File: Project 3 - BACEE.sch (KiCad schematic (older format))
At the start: 13 parts, among them U1 DS1337_PDv1, U2 24LC1025, U3 24LC1025, U4 ATMEGA328P-AU, Y1 Crystal, Y2 Crystal

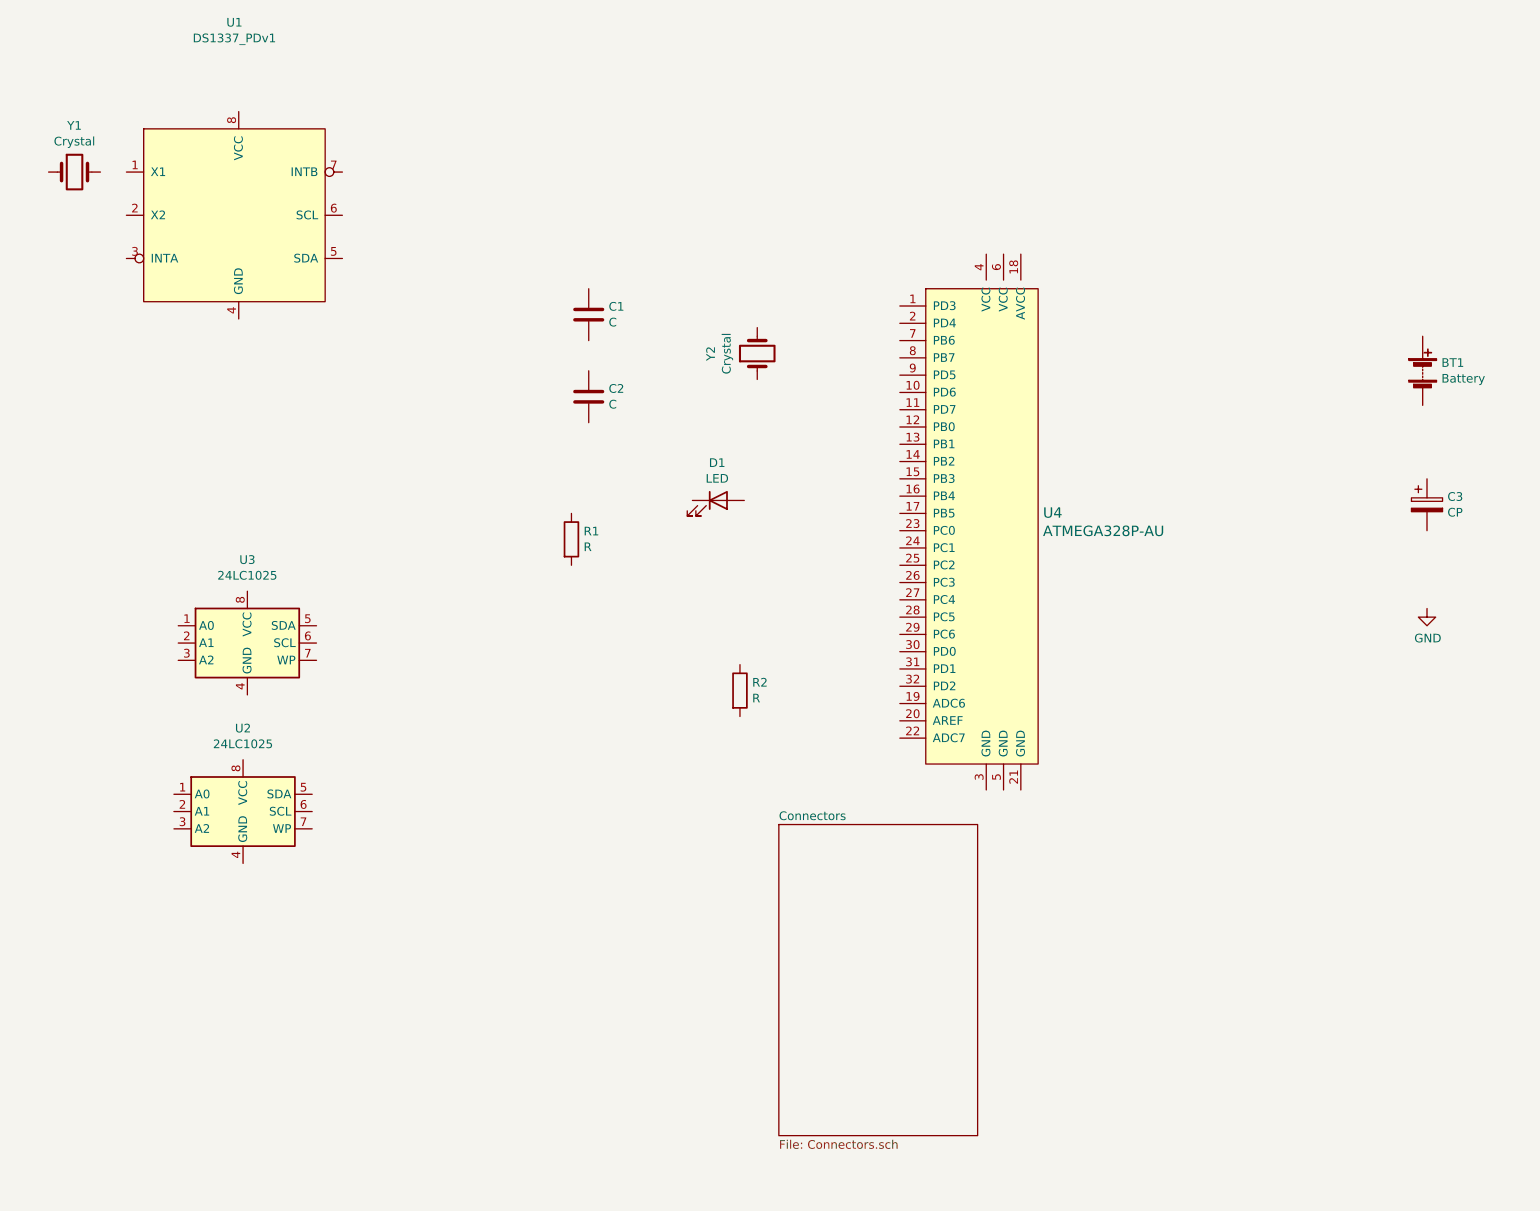
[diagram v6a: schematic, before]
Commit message: Completed association and added component values.
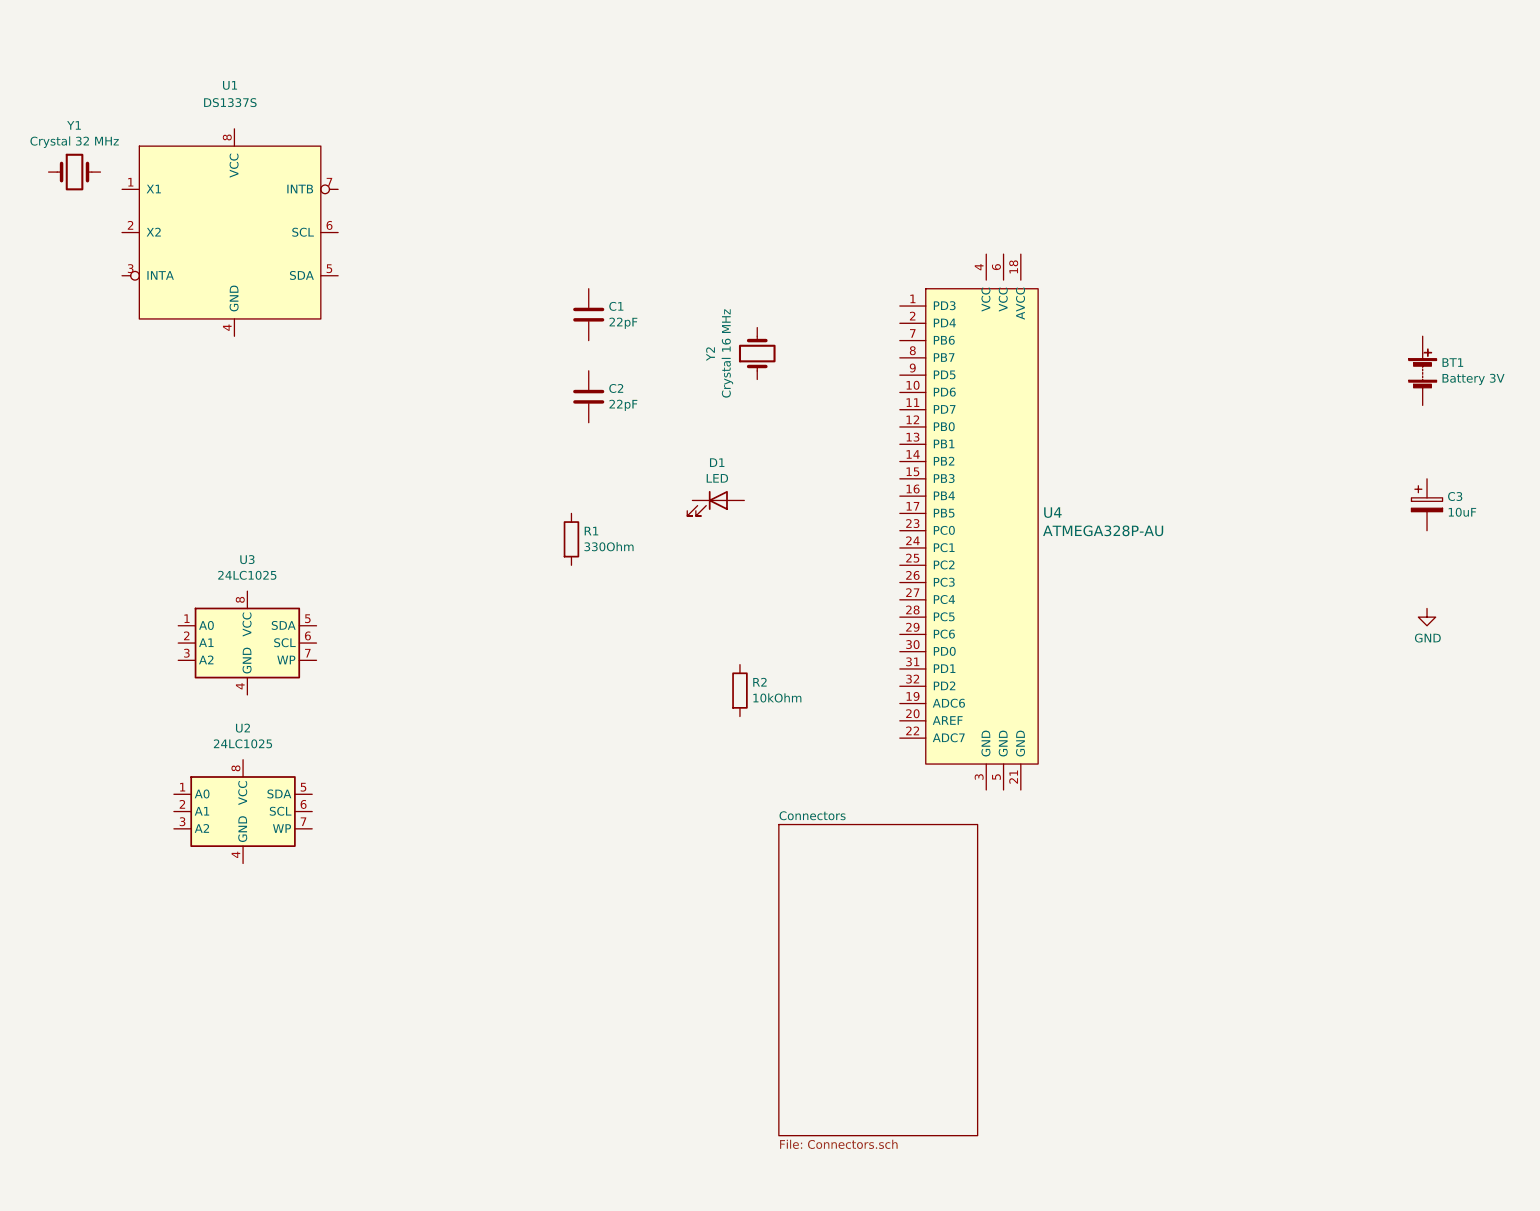
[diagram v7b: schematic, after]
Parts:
- BT1: value Battery -> Battery 3V; footprint (none) -> Connector_PinHeader_2.54mm:PinHeader_1x02_P2.54mm_Vertical
- C1, C2: value C -> 22pF; footprint (none) -> Capacitor_SMD:C_0805_2012Metric_Pad1.15x1.40mm_HandSolder
- C3: value CP -> 10uF; footprint (none) -> Capacitor_SMD:C_0805_2012Metric_Pad1.15x1.40mm_HandSolder
- D1: footprint (none) -> LED_SMD:LED_0805_2012Metric_Pad1.15x1.40mm_HandSolder
- R1: value R -> 330Ohm; footprint (none) -> Resistor_SMD:R_0805_2012Metric_Pad1.15x1.40mm_HandSolder
- R2: value R -> 10kOhm; footprint (none) -> Resistor_SMD:R_0805_2012Metric_Pad1.15x1.40mm_HandSolder
- U1: value DS1337_PDv1 -> DS1337S; footprint (none) -> Package_SO:SO-8_5.3x6.2mm_P1.27mm
- U2, U3: footprint (none) -> Package_SO:SOIJ-8_5.3x5.3mm_P1.27mm
- Y1: value Crystal -> Crystal 32 MHz; footprint (none) -> Crystal:Crystal_SMD_MicroCrystal_CC7V-T1A-2Pin_3.2x1.5mm
- Y2: value Crystal -> Crystal 16 MHz; footprint (none) -> Crystal:Crystal_SMD_5032-2Pin_5.0x3.2mm_HandSoldering
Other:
- moved on the sheet: U1
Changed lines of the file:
@@
 P 8900 2925
 F 0 "BT1" H 9008 2971 50  0000 L CNN
-F 1 "Battery" H 9008 2880 50  0000 L CNN
-F 2 "" V 8900 2985 50  0001 C CNN
+F 1 "Battery  3V" H 9008 2880 50  0000 L CNN
+F 2 "Connector_PinHeader_2.54mm:PinHeader_1x02_P2.54mm_Vertical" V 8900 2985 50  0001 C CNN
 F 3 "~" V 8900 2985 50  0001 C CNN
 	1    8900 2925
@@
 P 4075 2600
 F 0 "C1" H 4190 2646 50  0000 L CNN
-F 1 "C" H 4190 2555 50  0000 L CNN
-F 2 "" H 4113 2450 50  0001 C CNN
+F 1 "22pF" H 4190 2555 50  0000 L CNN
+F 2 "Capacitor_SMD:C_0805_2012Metric_Pad1.15x1.40mm_HandSolder" H 4113 2450 50  0001 C CNN
 F 3 "~" H 4075 2600 50  0001 C CNN
 	1    4075 2600
@@
 P 4075 3075
 F 0 "C2" H 4190 3121 50  0000 L CNN
-F 1 "C" H 4190 3030 50  0000 L CNN
-F 2 "" H 4113 2925 50  0001 C CNN
+F 1 "22pF" H 4190 3030 50  0000 L CNN
+F 2 "Capacitor_SMD:C_0805_2012Metric_Pad1.15x1.40mm_HandSolder" H 4113 2925 50  0001 C CNN
 F 3 "~" H 4075 3075 50  0001 C CNN
 	1    4075 3075
@@
 P 8925 3700
 F 0 "C3" H 9043 3746 50  0000 L CNN
-F 1 "CP" H 9043 3655 50  0000 L CNN
-F 2 "" H 8963 3550 50  0001 C CNN
+F 1 "10uF" H 9043 3655 50  0000 L CNN
+F 2 "Capacitor_SMD:C_0805_2012Metric_Pad1.15x1.40mm_HandSolder" H 8963 3550 50  0001 C CNN
 F 3 "~" H 8925 3700 50  0001 C CNN
 	1    8925 3700
@@
 F 0 "D1" H 4818 3892 50  0000 C CNN
 F 1 "LED" H 4818 3801 50  0000 C CNN
-F 2 "" H 4825 3675 50  0001 C CNN
+F 2 "LED_SMD:LED_0805_2012Metric_Pad1.15x1.40mm_HandSolder" H 4825 3675 50  0001 C CNN
 F 3 "~" H 4825 3675 50  0001 C CNN
 	1    4825 3675
@@
 P 3975 3900
 F 0 "R1" H 4045 3946 50  0000 L CNN
-F 1 "R" H 4045 3855 50  0000 L CNN
-F 2 "" V 3905 3900 50  0001 C CNN
+F 1 "330Ohm" H 4045 3855 50  0000 L CNN
+F 2 "Resistor_SMD:R_0805_2012Metric_Pad1.15x1.40mm_HandSolder" V 3905 3900 50  0001 C CNN
 F 3 "~" H 3975 3900 50  0001 C CNN
 	1    3975 3900
@@
 P 4950 4775
 F 0 "R2" H 5020 4821 50  0000 L CNN
-F 1 "R" H 5020 4730 50  0000 L CNN
-F 2 "" V 4880 4775 50  0001 C CNN
+F 1 "10kOhm" H 5020 4730 50  0000 L CNN
+F 2 "Resistor_SMD:R_0805_2012Metric_Pad1.15x1.40mm_HandSolder" V 4880 4775 50  0001 C CNN
 F 3 "~" H 4950 4775 50  0001 C CNN
 	1    4950 4775
@@
 F 0 "U3" H 2100 4981 50  0000 C CNN
 F 1 "24LC1025" H 2100 4890 50  0000 C CNN
-F 2 "" H 2100 4500 50  0001 C CNN
+F 2 "Package_SO:SOIJ-8_5.3x5.3mm_P1.27mm" H 2100 4500 50  0001 C CNN
 F 3 "http://ww1.microchip.com/downloads/en/DeviceDoc/21941B.pdf" H 2100 4500 50  0001 C CNN
 	1    2100 4500
@@
 L Project3:DS1337_PDv1 U1
 U 1 1 5F0DBCFF
-P 2050 2025
-F 0 "U1" H 2025 3140 50  0000 C CNN
-F 1 "DS1337_PDv1" H 2025 3049 50  0000 C CNN
-F 2 "" H 1750 2375 50  0001 C CNN
-F 3 "https://datasheets.maximintegrated.com/en/ds/DS1337-DS1337C.pdf" H 1750 2375 50  0001 C CNN
-	1    2050 2025
+P 2025 2125
+F 0 "U1" H 2000 2975 50  0000 C CNN
+F 1 "DS1337S" H 2000 2875 50  0000 C CNN
+F 2 "Package_SO:SO-8_5.3x6.2mm_P1.27mm" H 1725 2475 50  0001 C CNN
+F 3 "https://datasheets.maximintegrated.com/en/ds/DS1337-DS1337C.pdf" H 1725 2475 50  0001 C CNN
+	1    2025 2125
 	1    0    0    -1
 $EndComp
@@
 P 1100 1775
 F 0 "Y1" H 1100 2043 50  0000 C CNN
-F 1 "Crystal" H 1100 1952 50  0000 C CNN
-F 2 "" H 1100 1775 50  0001 C CNN
+F 1 "Crystal 32 MHz" H 1100 1952 50  0000 C CNN
+F 2 "Crystal:Crystal_SMD_MicroCrystal_CC7V-T1A-2Pin_3.2x1.5mm" H 1100 1775 50  0001 C CNN
 F 3 "~" H 1100 1775 50  0001 C CNN
 	1    1100 1775
@@
 P 5050 2825
 F 0 "Y2" H 5050 3093 50  0000 C CNN
-F 1 "Crystal" H 5050 3002 50  0000 C CNN
-F 2 "" H 5050 2825 50  0001 C CNN
+F 1 "Crystal 16 MHz" H 5050 3002 50  0000 C CNN
+F 2 "Crystal:Crystal_SMD_5032-2Pin_5.0x3.2mm_HandSoldering" H 5050 2825 50  0001 C CNN
 F 3 "~" H 5050 2825 50  0001 C CNN
 	1    5050 2825
@@
 F 0 "U2" H 2075 5956 50  0000 C CNN
 F 1 "24LC1025" H 2075 5865 50  0000 C CNN
-F 2 "" H 2075 5475 50  0001 C CNN
+F 2 "Package_SO:SOIJ-8_5.3x5.3mm_P1.27mm" H 2075 5475 50  0001 C CNN
 F 3 "http://ww1.microchip.com/downloads/en/DeviceDoc/21941B.pdf" H 2075 5475 50  0001 C CNN
 	1    2075 5475

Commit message: Completed wiring in connectors sheet
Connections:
- net GND: now also U4.21 (GND), U4.3 (GND), U4.5 (GND)
- net D3: now reaches U4.1 (PD3)
- net D6: now reaches U4.10 (PD6)
- net D7: now reaches U4.11 (PD7)
- net D8: now reaches U4.12 (PB0)
- net MOSI: now reaches U4.15 (PB3)
- net MISO: now reaches U4.16 (PB4)
- net SCK: now reaches U4.17 (PB5)
- net VCC: now reaches U4.18 (AVCC)
- net VCC: now also U4.4 (VCC), U4.6 (VCC)
- net D4: now reaches U4.2 (PD4)
- net SDA: now reaches U4.27 (PC4)
- net RESET: now reaches U4.29 (PC6)
- net RX: now reaches U4.30 (PD0)
- net TX: now reaches U4.31 (PD1)
- net D2: now reaches U4.32 (PD2)
- net D5: now reaches U4.9 (PD5)
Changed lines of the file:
@@
 	1    0    0    -1
 $EndComp
-$Sheet
-S 5175 5550 1150 1800
-U 5F0D3531
-F0 "Connectors" 50
-F1 "Connectors.sch" 50
-$EndSheet
 $Comp
 L dk_Embedded-Microcontrollers:ATMEGA328P-AU U4
@@
 U 1 1 5F0EA205
 P 5050 2825
-F 0 "Y2" H 5050 3093 50  0000 C CNN
-F 1 "Crystal 16 MHz" H 5050 3002 50  0000 C CNN
+F 0 "Y2" V 5425 2825 50  0000 C CNN
+F 1 "Crystal 16 MHz" V 5300 2825 50  0000 C CNN
 F 2 "Crystal:Crystal_SMD_5032-2Pin_5.0x3.2mm_HandSoldering" H 5050 2825 50  0001 C CNN
 F 3 "~" H 5050 2825 50  0001 C CNN
@@
 	1    0    0    -1
 $EndComp
+Text HLabel 4700 5825 2    50   Input ~ 0
+MISO
+Text Label 4500 5825 2    50   ~ 0
+MISO
+Wire Wire Line
+	4700 5825 4500 5825
+Text Label 5875 3650 2    50   ~ 0
+MISO
+$Sheet
+S 4700 5575 1150 1800
+U 5F0D3531
+F0 "Connectors" 50
+F1 "Connectors.sch" 50
+F2 "SCK" B L 4700 6125 50
+F3 "RESET" O L 4700 6275 50
+F4 "VCC" I L 4700 6950 50
+F5 "MOSI" I L 4700 5975 50
+F6 "GND" I L 4700 7100 50
+F7 "RX" I L 4700 6500 50
+F8 "TX" O L 4700 6625 50
+F9 "SDA" B R 5850 5775 50
+F10 "D2" B R 5850 6275 50
+F11 "D3" B R 5850 6400 50
+F12 "D4" B R 5850 6525 50
+F13 "D5" B R 5850 6650 50
+F14 "D6" B R 5850 6775 50
+F15 "D7" B R 5850 6900 50
+F16 "D8" B R 5850 7025 50
+$EndSheet
+Text Label 4500 5975 2    50   ~ 0
+MOSI
+Text Label 4500 6125 2    50   ~ 0
+SCK
+Text Label 4500 6275 2    50   ~ 0
+RESET
+Text Label 4500 6950 2    50   ~ 0
+VCC
+Text Label 4500 7100 2    50   ~ 0
+GND
+Wire Wire Line
+	4700 5975 4500 5975
+Wire Wire Line
+	4700 6125 4500 6125
+Wire Wire Line
+	4700 6950 4500 6950
+Wire Wire Line
+	4500 6275 4700 6275
+Wire Wire Line
+	4500 7100 4600 7100
+Text Label 5875 3550 2    50   ~ 0
+MOSI
+Text Label 5875 3750 2    50   ~ 0
+SCK
+Text Label 5875 4450 2    50   ~ 0
+RESET
+Text Label 6475 1975 2    50   ~ 0
+VCC
+Wire Wire Line
+	6375 2250 6375 2125
+Wire Wire Line
+	6375 2125 6475 2125
+Wire Wire Line
+	6575 2125 6575 2250
+Wire Wire Line
+	6475 2250 6475 2125
+Connection ~ 6475 2125
+Wire Wire Line
+	6475 2125 6575 2125
+Wire Wire Line
+	6475 1975 6475 2125
+Wire Wire Line
+	6375 5350 6375 5500
+Wire Wire Line
+	6375 5500 6475 5500
+Wire Wire Line
+	6575 5500 6575 5350
+Connection ~ 6475 5500
+Wire Wire Line
+	6475 5500 6575 5500
+Wire Wire Line
+	6475 5350 6475 5500
+Text Label 6475 5700 2    50   ~ 0
+GND
+Wire Wire Line
+	6475 5500 6475 5700
+$Comp
+L power:GNDPWR #PWR?
+U 1 1 5F101DCC
+P 4500 7500
+F 0 "#PWR?" H 4500 7300 50  0001 C CNN
+F 1 "GNDPWR" H 4504 7346 50  0000 C CNN
+F 2 "" H 4500 7450 50  0001 C CNN
+F 3 "" H 4500 7450 50  0001 C CNN
+	1    4500 7500
+	1    0    0    -1
+$EndComp
+Wire Wire Line
+	4500 7500 4500 7200
+Wire Wire Line
+	4500 7200 4600 7200
+Wire Wire Line
+	4600 7200 4600 7100
+Connection ~ 4600 7100
+Wire Wire Line
+	4600 7100 4700 7100
+Text Label 6150 5775 0    50   ~ 0
+SDA
+Text Label 6150 6275 0    50   ~ 0
+D2
+Text Label 6150 6400 0    50   ~ 0
+D3
+Text Label 6150 6525 0    50   ~ 0
+D4
+Text Label 6150 6650 0    50   ~ 0
+D5
+Text Label 6150 6775 0    50   ~ 0
+D6
+Text Label 6150 6900 0    50   ~ 0
+D7
+Text Label 6150 7025 0    50   ~ 0
+D8
+Text Label 4500 6500 2    50   ~ 0
+RX
+Text Label 4500 6625 2    50   ~ 0
+TX
+Wire Wire Line
+	5850 6275 6150 6275
+Wire Wire Line
+	6150 6400 5850 6400
+Wire Wire Line
+	5850 6525 6150 6525
+Wire Wire Line
+	6150 6650 5850 6650
+Wire Wire Line
+	5850 6775 6150 6775
+Wire Wire Line
+	5850 6900 6150 6900
+Wire Wire Line
+	6150 7025 5850 7025
+Wire Wire Line
+	5850 5775 6150 5775
+Wire Wire Line
+	4500 6500 4700 6500
+Wire Wire Line
+	4700 6625 4500 6625
+Text Label 5875 2550 2    50   ~ 0
+D3
+Text Label 5875 2650 2    50   ~ 0
+D4
+Text Label 5875 2950 2    50   ~ 0
+D5
+Text Label 5875 3050 2    50   ~ 0
+D6
+Text Label 5875 3150 2    50   ~ 0
+D7
+Text Label 5875 3250 2    50   ~ 0
+D8
+Text Label 5875 4250 2    50   ~ 0
+SDA
+Text Label 5875 4550 2    50   ~ 0
+RX
+Text Label 5875 4650 2    50   ~ 0
+TX
+Text Label 5875 4750 2    50   ~ 0
+D2
 $EndSCHEMATC
